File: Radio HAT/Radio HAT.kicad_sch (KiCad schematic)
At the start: 24 parts, among them J1 Raspberry_Pi_2_3, J2 Coax SMA, J3 Barrel_Jack, J4 VCC, J5 6V, J6 GND, U1 RFM98PW, U2 AZ2185D-ADJTRG1

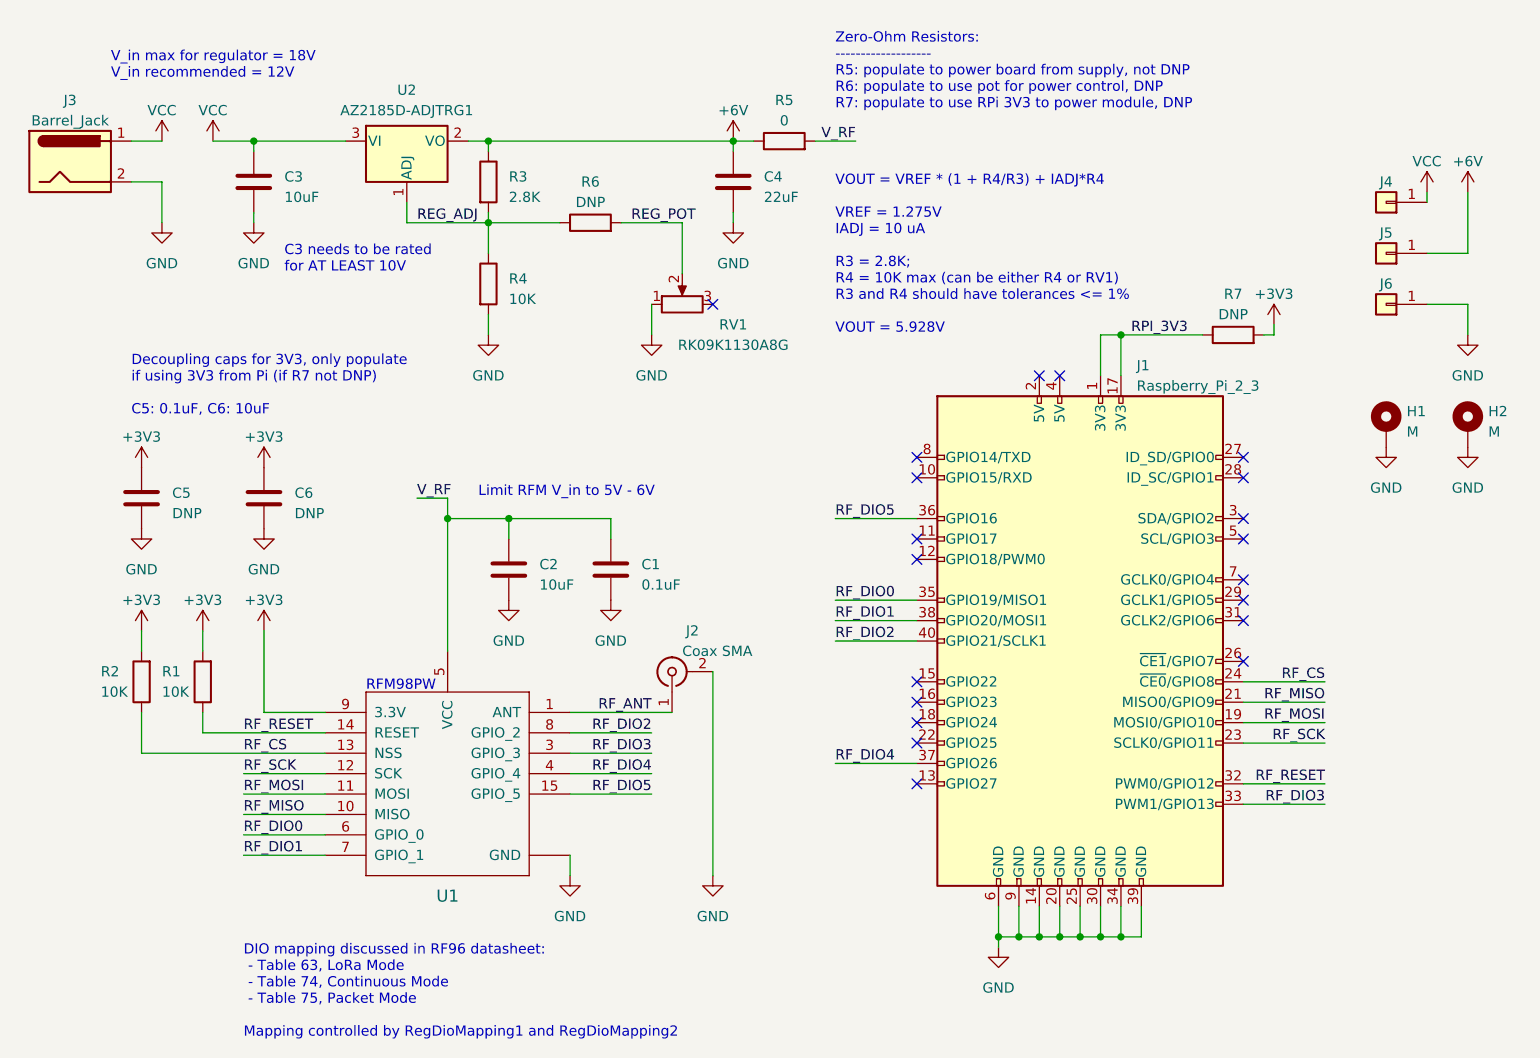
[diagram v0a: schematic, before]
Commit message: Updated copper pours
Copper pours had gone out of alignment, reworked and increased sizes
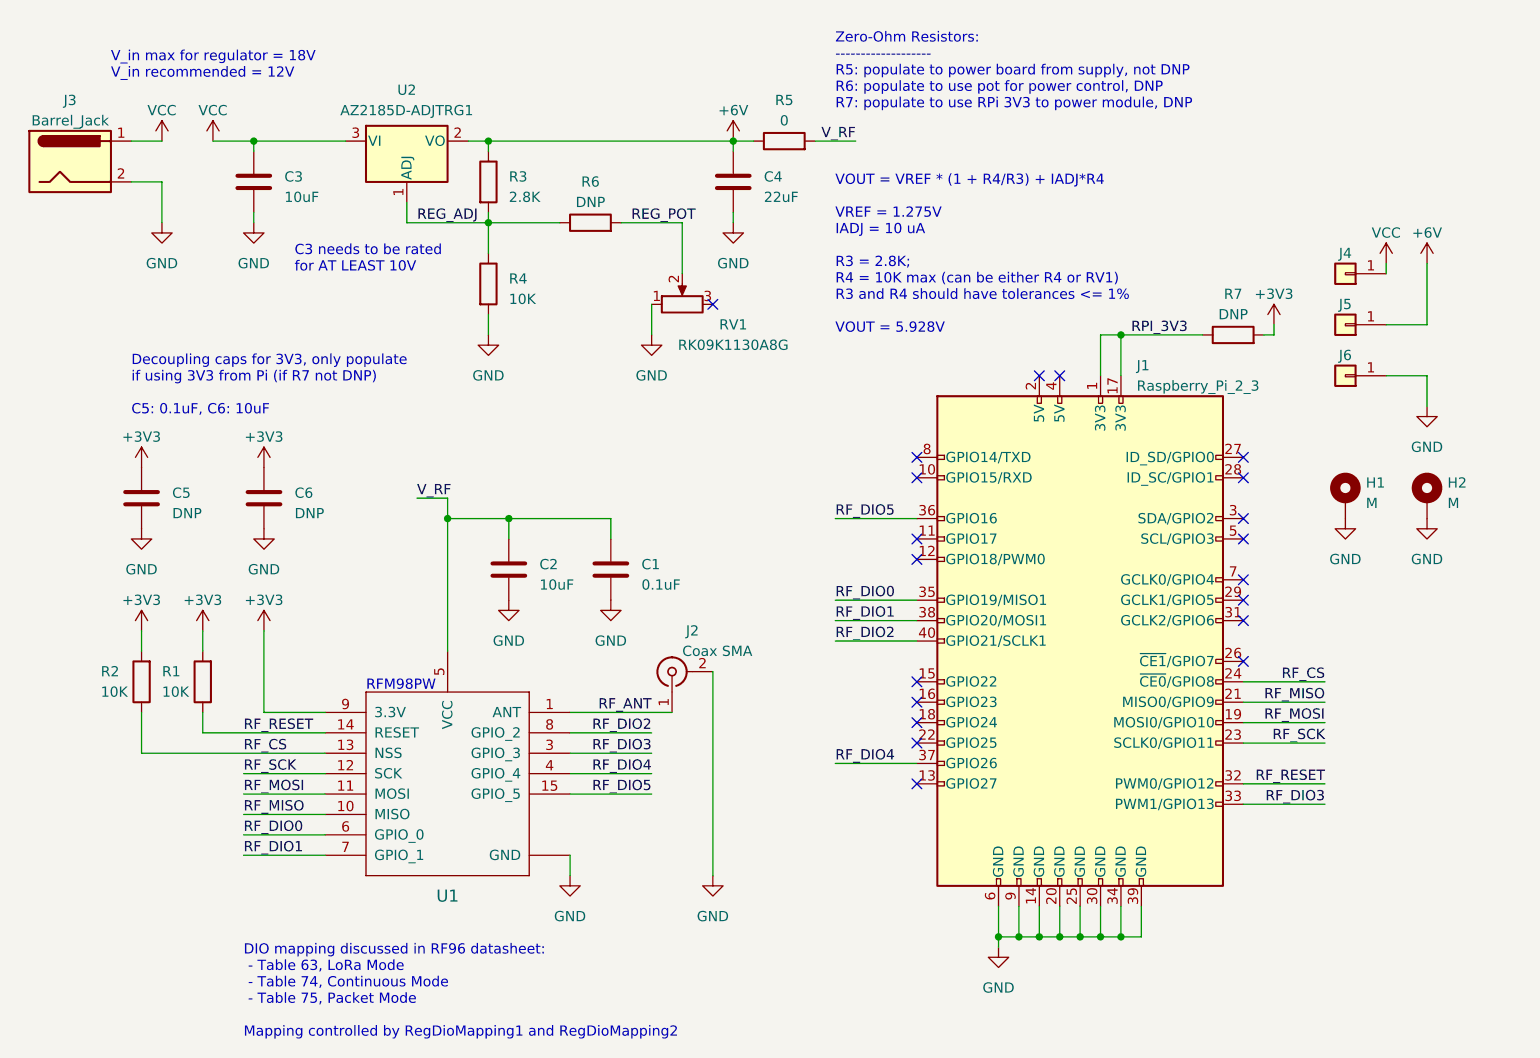
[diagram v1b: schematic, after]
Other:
- note removed: "Limit RFM V_in to 5V - 6V"
- moved on the sheet: H1, H2, J4, J5, J6

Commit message: Converted to 4-layer board
Changes:
- added 2 internal layers
- stackup: PWR - GND - SIG - GND
- added POW indicator LED
- increased density of stitching vias
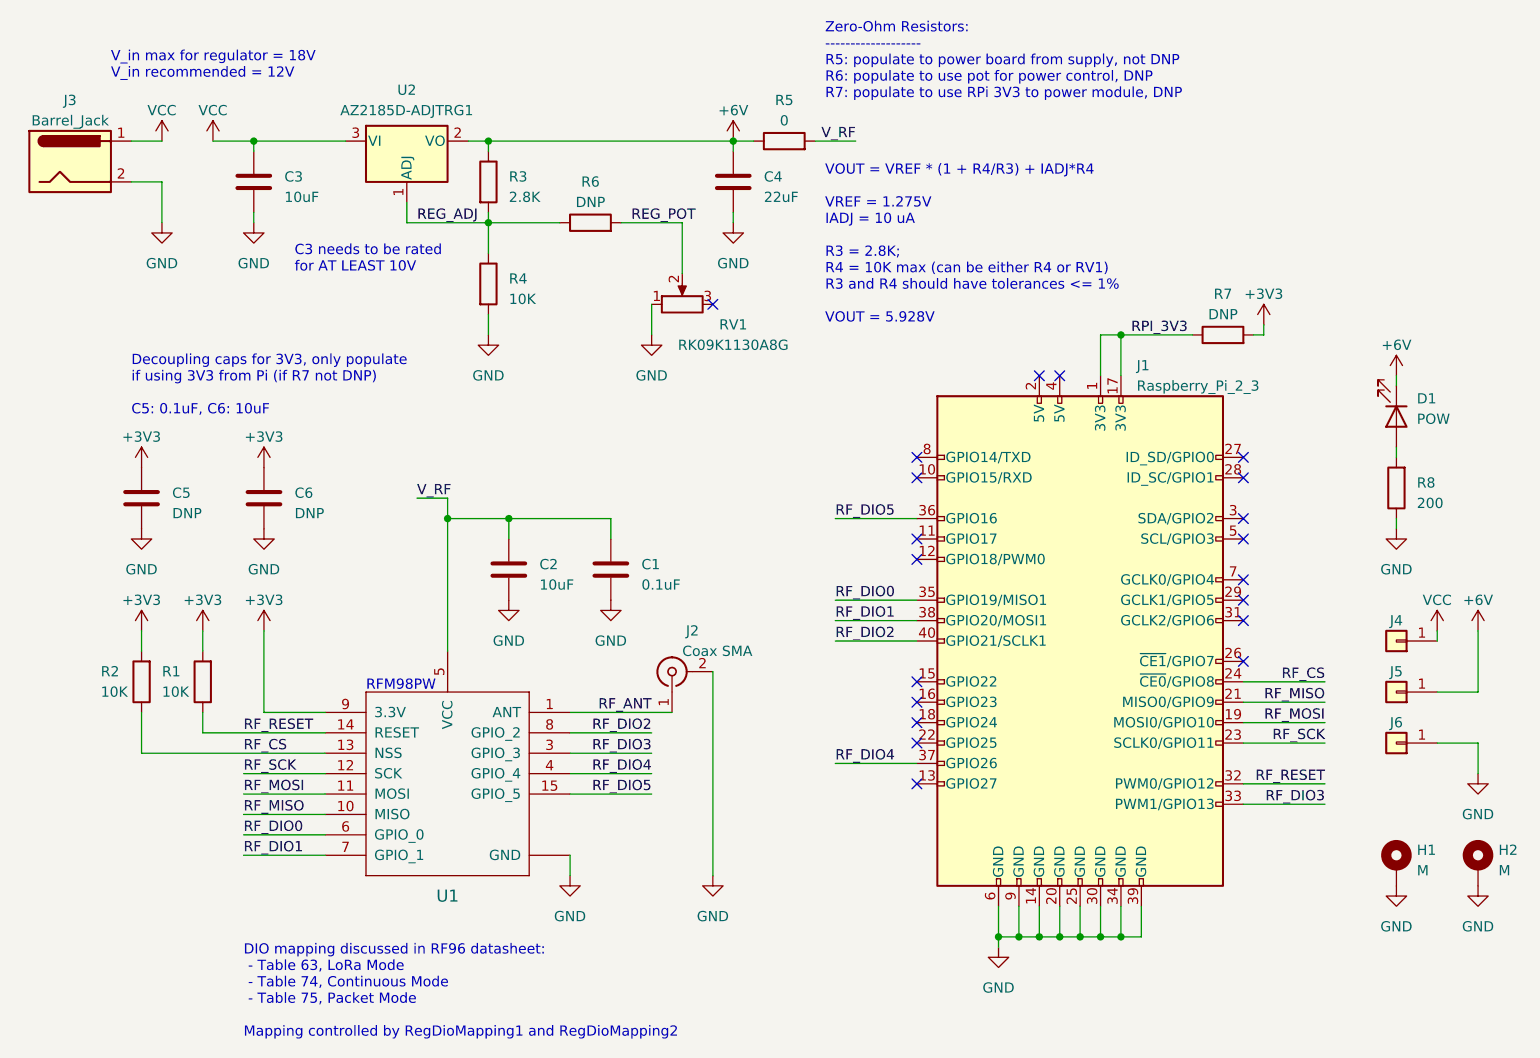
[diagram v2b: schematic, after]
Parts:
- added D1: POW, LED_SMD:LED_0805_2012Metric_Pad1.15x1.40mm_HandSolder, symbol Device:LED
- added R8: 200, Resistor_SMD:R_0805_2012Metric_Pad1.20x1.40mm_HandSolder, symbol Device:R
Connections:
- net +6V: now also D1.1 (K)
- net GND: now also R8.1
- new net: D1.2 (A), R8.2
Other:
- moved on the sheet: H1, H2, J4, J5, J6, R7

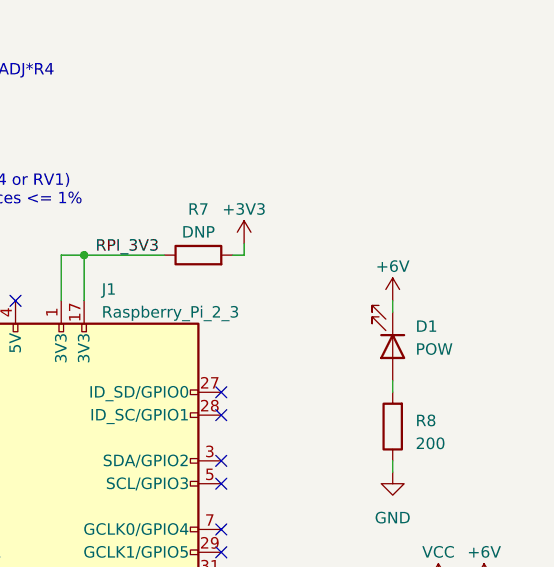
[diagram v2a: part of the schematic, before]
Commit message: Changed layer stackup
Board is now GND-PWR-SIG-GND to shield nets from interference from top and bottom
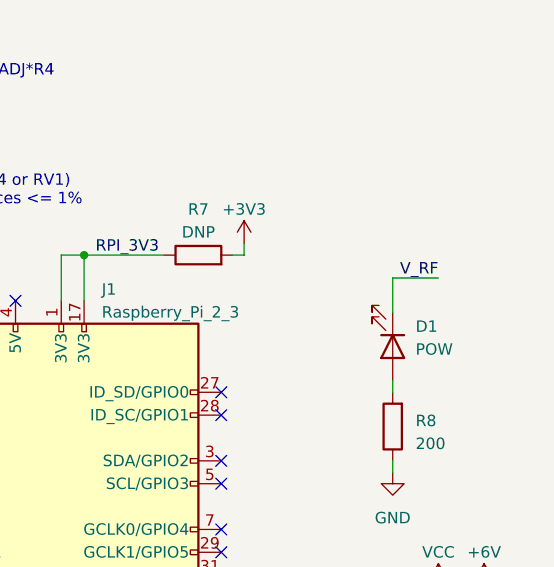
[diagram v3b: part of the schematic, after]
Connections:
- net +6V: no longer D1.1 (K)
- net V_RF: now also D1.1 (K)
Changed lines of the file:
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@@
   (title_block
     (title "Argus-1 Ground Station")
-    (date "2023-10-31")
+    (date "2023-11-01")
     (rev "v1.1")
     (company "LICENSE: CC BY 4.0")
@@
     (stroke (width 0) (type default))
   )
+  (wire (pts (xy 217.17 69.85) (xy 222.25 69.85))
+    (stroke (width 0) (type default))
+  )
   (wire (pts (xy 114.3 116.84) (xy 124.46 116.84))
     (stroke (width 0) (type default))
@@
     (stroke (width 0) (type default))
   )
-  (wire (pts (xy 217.17 72.39) (xy 217.17 73.66))
+  (wire (pts (xy 217.17 69.85) (xy 217.17 73.66))
     (stroke (width 0) (type default))
   )
@@
   )
   (label "RF_DIO2" (at 124.46 116.84 180) (fields_autoplaced)
+    (effects (font (size 1.27 1.27)) (justify right bottom))
+  )
+  (label "V_RF" (at 222.25 69.85 180) (fields_autoplaced)
     (effects (font (size 1.27 1.27)) (justify right bottom))
   )
@@
         )
       )
-    )
-  )
-  (symbol (lib_id "power:+6V") (at 217.17 72.39 0) (unit 1)
-    (in_bom yes) (on_board yes) (dnp no) (fields_autoplaced)
-    (property "Reference" "#PWR027" (at 217.17 76.2 0)
-      (effects (font (size 1.27 1.27)) hide)
-    )
-    (property "Value" "+6V" (at 217.17 68.58 0)
-      (effects (font (size 1.27 1.27)))
-    )
-    (property "Footprint" "" (at 217.17 72.39 0)
-      (effects (font (size 1.27 1.27)) hide)
-    )
-    (property "Datasheet" "" (at 217.17 72.39 0)
-      (effects (font (size 1.27 1.27)) hide)
-    )
-    (pin "1")
-    (instances
-      (project "Radio HAT"
-        (path "/e833ba5c-90ae-4111-9eec-1a872963763a"
-          (reference "#PWR027") (unit 1)
-        )
-      )
